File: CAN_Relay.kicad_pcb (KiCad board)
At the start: 2 copper layers, 91.4 x 66 mm, 42 parts, among them J1 430450601, J2 BCS-114-L-S-PE-BE, J3 BCS-114-L-S-PE-BE, J4 691305340008, J5 691305340008, U2 BTS716GB, U3 BTS716GB, U4 ADM3057EBRWZ, U5 LM22676MRE-5.0/NOPB

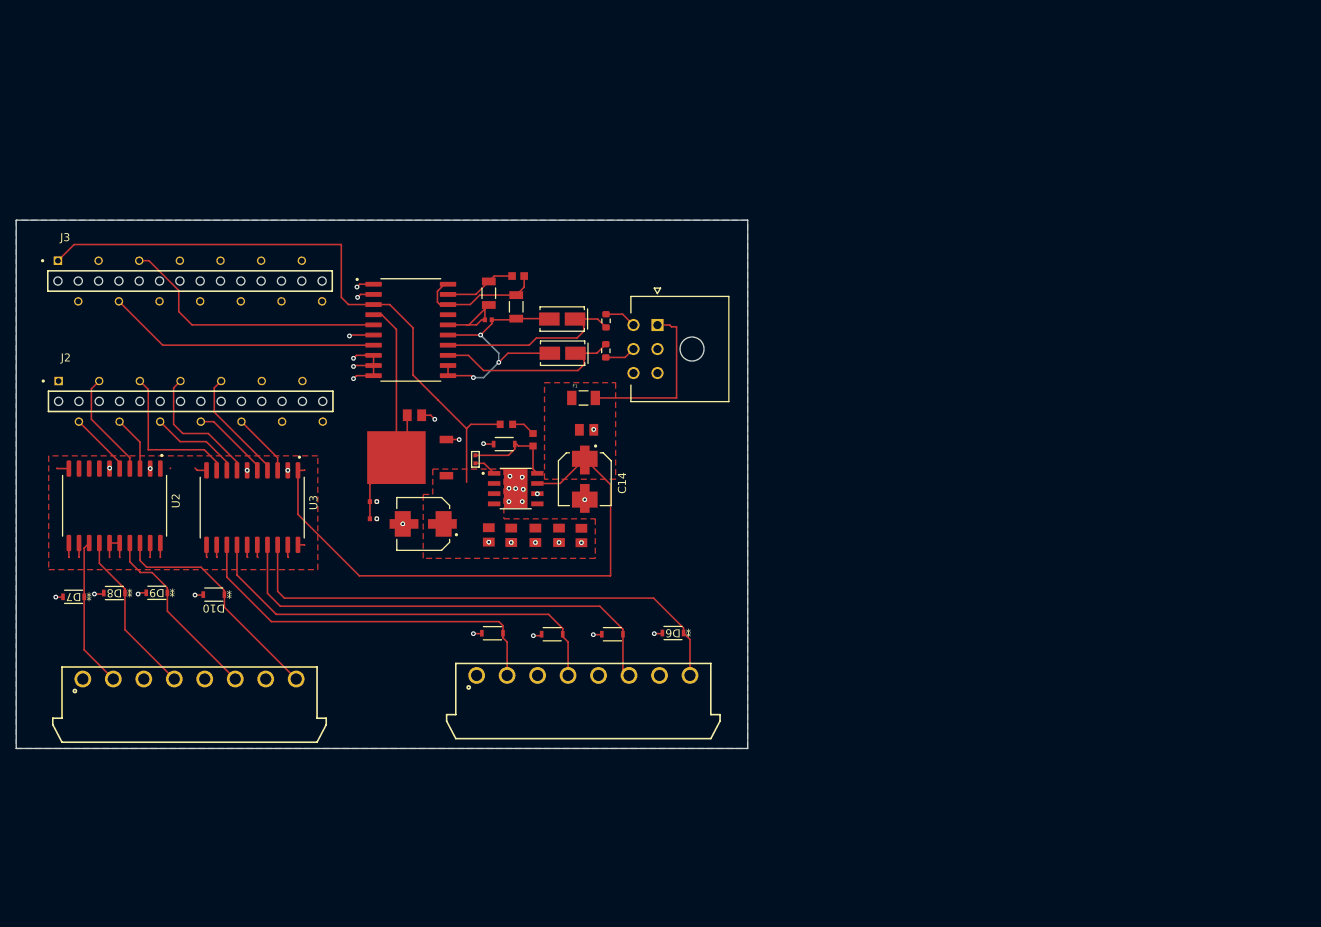
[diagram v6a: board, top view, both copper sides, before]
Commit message: Redid CAN side of PCB to replace Buck Converter
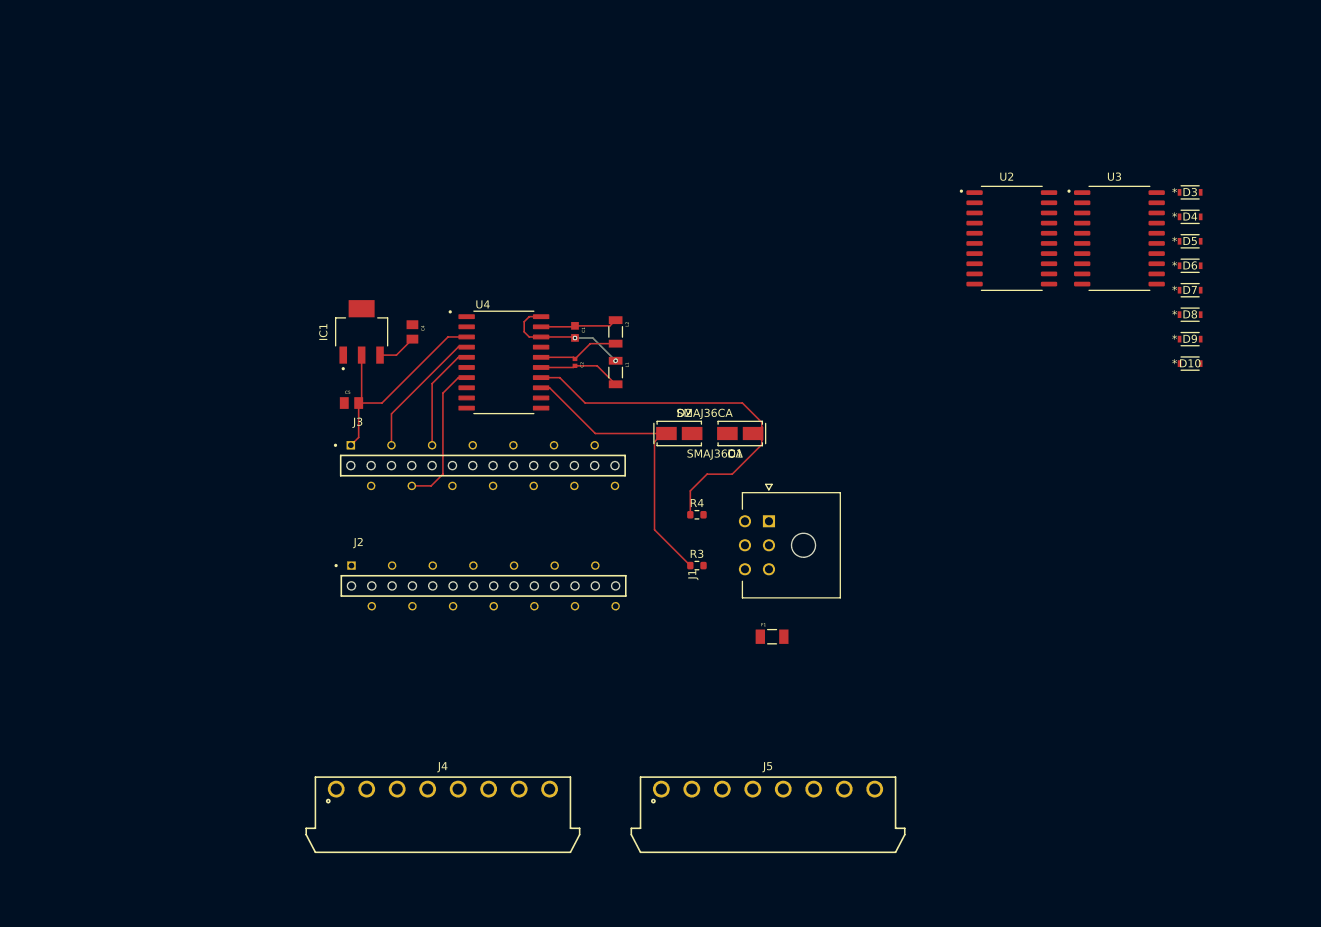
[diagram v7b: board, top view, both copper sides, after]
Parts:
- removed C10, C11, C12, C13, C3: C, Cap10U:CAPC2012X145N
- removed C14, C9: C_Polarized_US, EEEFT1V101AV:CAP_EEEFT1V101AV
- removed C6, C7: 1U, GRT155C80J105KE01J:CAPC1005X55N
- removed C8: 100N, WCAP-CSGP_0402:WCAP-CSGP_0402
- removed CR1: LF33CDT-TR, LF33CDT-TR:TO228P972X240-3N
- removed D11: D, RRE02VTM4SFHTR:DIO_RRE02VSM_ROM
- removed L3, L4: L, LQM18FN100M00D:INDC1608X90N
- removed U5: LM22676MRE-5.0/NOPB, LM22676MRE-5.0_NOPB:VREG_LM5017MR_NOPB
- added IC1: REG1117-5, REG1117-5:SOT230P700X180-4N, F.Cu at (106.7, 80.0)
- moved D7 144.7 mm to (210.2, 74.8), turned to 0 degrees
- moved D8 138.9 mm to (210.2, 77.9), turned to 0 degrees
- moved D9 133.0 mm to (210.2, 80.9), turned to 0 degrees
- moved D10 125.4 mm to (210.2, 84.0), turned to 0 degrees
- moved U2 117.0 mm to (187.9, 68.3), turned to 0 degrees
- moved U3 113.5 mm to (201.4, 68.3), turned to 0 degrees
- moved D3 103.2 mm to (210.2, 62.6), turned to 0 degrees
- moved D4 95.3 mm to (210.2, 65.6), turned to 0 degrees
- moved D5 87.3 mm to (210.2, 68.7), turned to 0 degrees
- moved D6 79.3 mm to (210.2, 71.7), turned to 0 degrees
- moved J2 43.3 mm to (121.9, 111.8)
- moved J3 43.3 mm to (121.8, 96.7)
- moved F1 38.0 mm to (158.0, 118.1)
- moved J4 34.5 mm to (116.8, 137.2)
- moved C5 33.2 mm to (105.4, 88.9), turned to 0 degrees
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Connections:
- C4 pad 1: +5 -> GND
- C4 pad 2: GND -> +12
- C5 pad 1: +5 -> GND
- C5 pad 2: GND -> +5
- J3 pad 03: unconnected-(J3-Pad03) -> +3.3
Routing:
- net +12: track 96.0 -> 4.88 mm
- net Net-(D6-K): track 64.7 -> 0.00 mm
- net Net-(D5-K): track 58.4 -> 0.00 mm
- net Net-(D4-K): track 53.4 -> 0.00 mm
- net +5: track 79.9 -> 28.7 mm
- net Net-(D3-K): track 47.5 -> 0.00 mm
- net GND: track 32.5 -> 0.00 mm, vias 39 -> 0
- net Net-(D10-K): track 29.1 -> 0.00 mm
- net /CaNHi: track 24.1 -> 47.9 mm
- net Net-(D9-K): track 23.3 -> 0.00 mm
- net /GNDCan: track 33.5 -> 10.4 mm, vias 3 -> 0
- net Net-(F1-Pad2): track 21.5 -> 0.00 mm
- net Net-(D8-K): track 20.9 -> 0.00 mm
- net /CANRX: track 34.2 -> 13.4 mm
- net Net-(U3-IN4): track 19.2 -> 0.00 mm
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- removed copper zone on F.Cu, net +12
- removed copper zone on F.Cu, net +5
- removed copper zone on B.Cu, net GND
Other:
- board outline removed

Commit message: Connected everything, need to set trace size
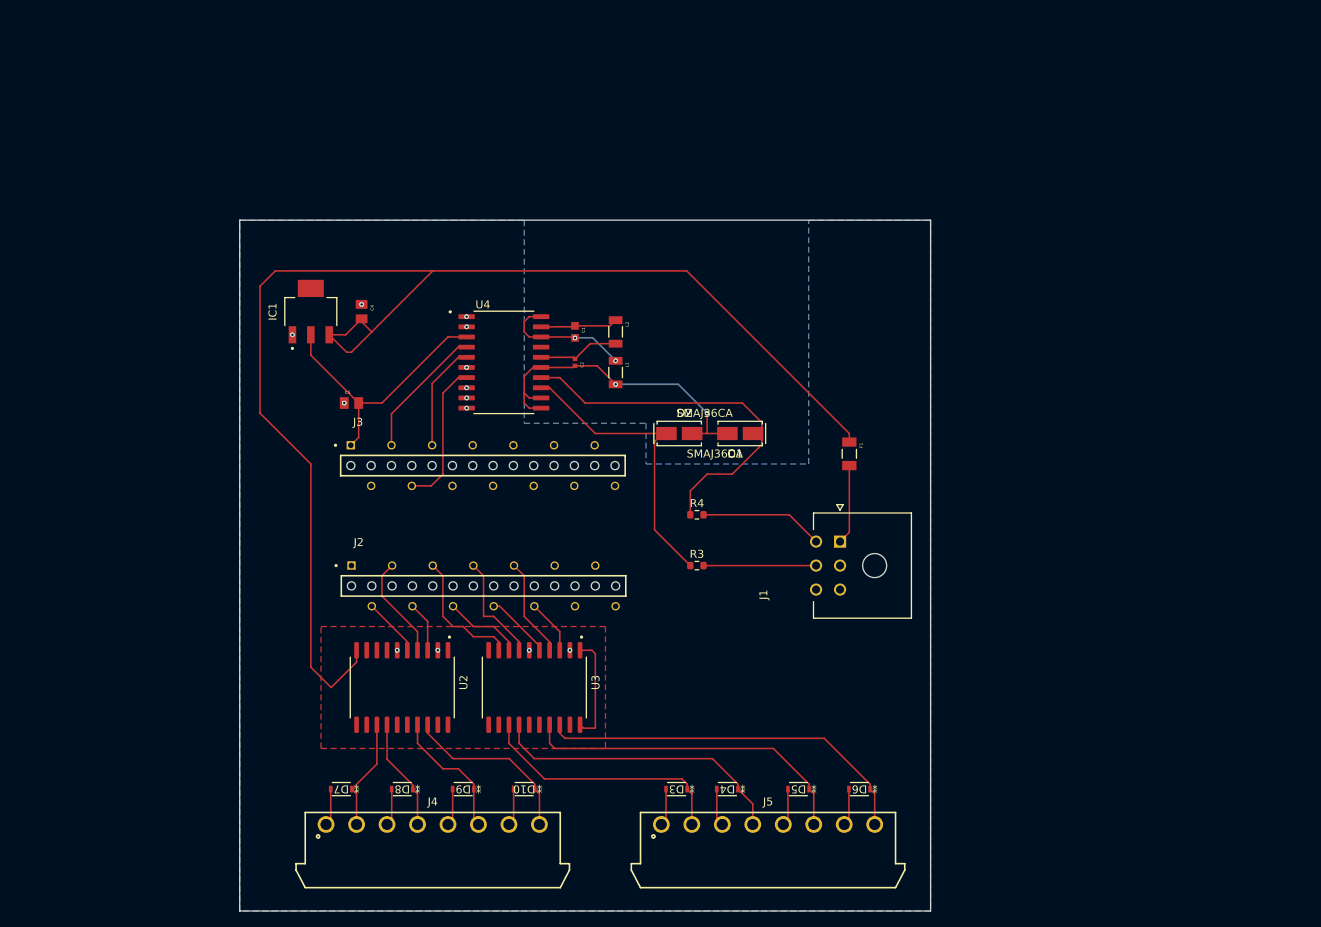
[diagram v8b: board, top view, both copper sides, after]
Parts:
- moved D7 123.1 mm to (104.1, 137.2), turned to 180 degrees
- moved D8 115.0 mm to (111.8, 137.2), turned to 180 degrees
- moved D9 106.9 mm to (119.4, 137.2), turned to 180 degrees
- moved D10 98.8 mm to (127.0, 137.2), turned to 180 degrees
- moved D3 98.4 mm to (146.1, 137.2), turned to 180 degrees
- moved U2 94.6 mm to (111.8, 124.5), turned to -90 degrees
- moved U3 92.2 mm to (128.3, 124.5), turned to -90 degrees
- moved D4 92.0 mm to (152.4, 137.2), turned to 180 degrees
- moved D5 84.2 mm to (161.3, 137.2), turned to 180 degrees
- moved D6 77.4 mm to (168.9, 137.2), turned to 180 degrees
- moved F1 24.8 mm to (167.6, 95.2), turned to -90 degrees
- moved J1 9.25 mm to (166.5, 106.2)
- moved IC1 6.84 mm to (100.3, 77.5)
- moved C4 6.84 mm to (106.7, 77.5)
- moved J4 4.60 mm to (115.6, 141.6)
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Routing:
- net +12: track 4.88 -> 182.3 mm
- net Net-(D6-K): track 0.00 -> 47.8 mm
- net Net-(D5-K): track 0.00 -> 42.2 mm
- net Net-(D4-K): track 0.00 -> 37.6 mm
- net GND: track 0.00 -> 37.3 mm, vias 0 -> 13
- net Net-(D3-K): track 0.00 -> 32.0 mm
- net /GNDCan: track 10.4 -> 40.9 mm, vias 0 -> 2
- net Net-(D10-K): track 0.00 -> 22.4 mm
- net Net-(D9-K): track 0.00 -> 16.8 mm
- net Net-(U3-IN4): track 0.00 -> 16.2 mm
- net /CaNH: track 0.00 -> 15.5 mm
- net /CaNL: track 0.00 -> 14.1 mm
- net Net-(D8-K): track 0.00 -> 14.0 mm
- net Net-(D7-K): track 0.00 -> 14.0 mm
- net Net-(U3-IN3): track 0.00 -> 13.7 mm
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- added copper zone on F.Cu, net +12
- added copper zone on B.Cu, net GND
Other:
- board outline added: 86.4 x 86.4 mm
